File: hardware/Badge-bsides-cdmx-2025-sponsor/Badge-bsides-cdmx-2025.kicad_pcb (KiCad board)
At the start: 2 copper layers, 50 x 110 mm, 30 parts, among them J1 SWDIO, J3 ADDON, J4 Conn_01x04_Pin, J5 I2C, J6 Conn_01x04_Pin, P6 USB_C_Plug_USB2.0, Q3 DMG3415U-7, SW11 ON, SW2 RESET, U1 PY32F030F28U6TR, U6 AP2112K-3.3

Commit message: feat(Hw):started_routing
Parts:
- added C67: 10uF, Capacitor_SMD:C_0603_1608Metric, B.Cu at (-18.5, 29.3)
- added C68: 10uF, Capacitor_SMD:C_0603_1608Metric, B.Cu at (-9.79, 28.9)
- added C69: 10uF, Capacitor_SMD:C_0603_1608Metric, B.Cu at (-27.7, 29.1)
- added C70: 10uF, Capacitor_SMD:C_0603_1608Metric, B.Cu at (-37.4, 30.7)
- added R5: 10k, Resistor_SMD:R_0603_1608Metric, B.Cu at (-18.5, 30.8)
- added R6: 10k, Resistor_SMD:R_0603_1608Metric, B.Cu at (-9.79, 30.4)
- added R7: 10k, Resistor_SMD:R_0603_1608Metric, B.Cu at (-27.7, 30.6)
- added R8: 10k, Resistor_SMD:R_0603_1608Metric, B.Cu at (-37.4, 29.2)
- added SW10: SW_Push, Footprints:TS1088R02026, F.Cu at (-37.3, 29.9)
- added SW7: SW_Push, Footprints:TS1088R02026, F.Cu at (-27.8, 29.9)
- added SW8: SW_Push, Footprints:TS1088R02026, F.Cu at (-18.6, 29.9)
- added SW9: SW_Push, Footprints:TS1088R02026, F.Cu at (-9.34, 29.9)
- BT3, BT4: moved to B.Cu
- J3: moved to F.Cu
- J4: footprint Connector_PinHeader_2.54mm:PinHeader_1x04_P2.54mm_Vertical -> Connector_PinHeader_2.54mm:PinHeader_1x04_P2.54mm_Horizontal; moved to B.Cu
- J6: footprint Connector_PinHeader_2.54mm:PinHeader_1x04_P2.54mm_Vertical -> Connector_PinSocket_2.54mm:PinSocket_1x04_P2.54mm_Horizontal; moved to B.Cu
- moved J1 223.1 mm to (-47.3, 40.9)
- moved J3 190.4 mm to (-44.2, 6.08), turned to 90 degrees
- moved R11 185.4 mm to (-24.3, 41.3), turned to 180 degrees
- moved C33 180.0 mm to (-12.3, 65.4)
- moved D10 179.8 mm to (-24.4, 44.0)
- moved D9 179.8 mm to (-24.1, 67.7), turned to 0 degrees
- moved F3 179.7 mm to (-12.3, 68.4)
- moved J5 179.6 mm to (-47.3, 16.2)
- moved D4 179.5 mm to (-42.1, 71.7)
- moved P6 179.5 mm to (-6.99, 70.8)
- moved Q3 179.5 mm to (-41.6, 75.9)
- moved R10 179.5 mm to (-44.4, 75.9)
- moved SW11 179.5 mm to (-46.7, 70.3)
- moved U1 179.5 mm to (-25.6, 52.5)
- moved C10 179.4 mm to (-37.5, 69.3)
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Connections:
- BT3 pad 2: +3.3V -> +BATT
- J3 pad 5: /GPIO1 -> /GPIO2
- J3 pad 6: /GPIO2 -> /GPIO1
- J4 pad 1: /RX -> GND
- J4 pad 2: /RX -> GND
- J4 pad 3: GND -> /RX
- J4 pad 4: GND -> /RX
- J6 pad 1: /TX -> GND
- J6 pad 2: /TX -> GND
- J6 pad 3: GND -> /TX
- J6 pad 4: GND -> /TX
- U1 pad 1: unconnected-(U1-PA5-Pad1) -> /BTTN2
- U1 pad 10: unconnected-(U1-PB6-Pad10) -> /LED1
- U1 pad 16: /GPIO2 -> /BTTN4
- U1 pad 17: /GPIO1 -> /BTTN3
- U1 pad 2: /LED1 -> /BTTN1
- U1 pad 20: unconnected-(U1-PA4-Pad20) -> /LED2
- U1 pad 3: /LED2 -> /GPIO1
- U1 pad 5: unconnected-(U1-PA12-Pad5) -> /GPIO2
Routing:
- net Net-(BT3--): track 0.00 -> 55.1 mm
- net VBUS: track 0.00 -> 40.2 mm, vias 0 -> 2
- net +BATT: track 0.00 -> 16.9 mm
- net Net-(SW11-A): track 0.00 -> 14.8 mm
- net Net-(F3-Pad1): track 0.00 -> 10.8 mm
- net Net-(D4-K): track 0.00 -> 9.51 mm
- net Net-(P6-CC): track 0.00 -> 7.73 mm
- net Net-(P6-VCONN): track 0.00 -> 6.86 mm
- net +3V3: track 0.00 -> 1.80 mm
- net /BTTN2: track 0.00 -> 1.52 mm
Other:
- board size 50 x 110 mm -> 50.1 x 110 mm

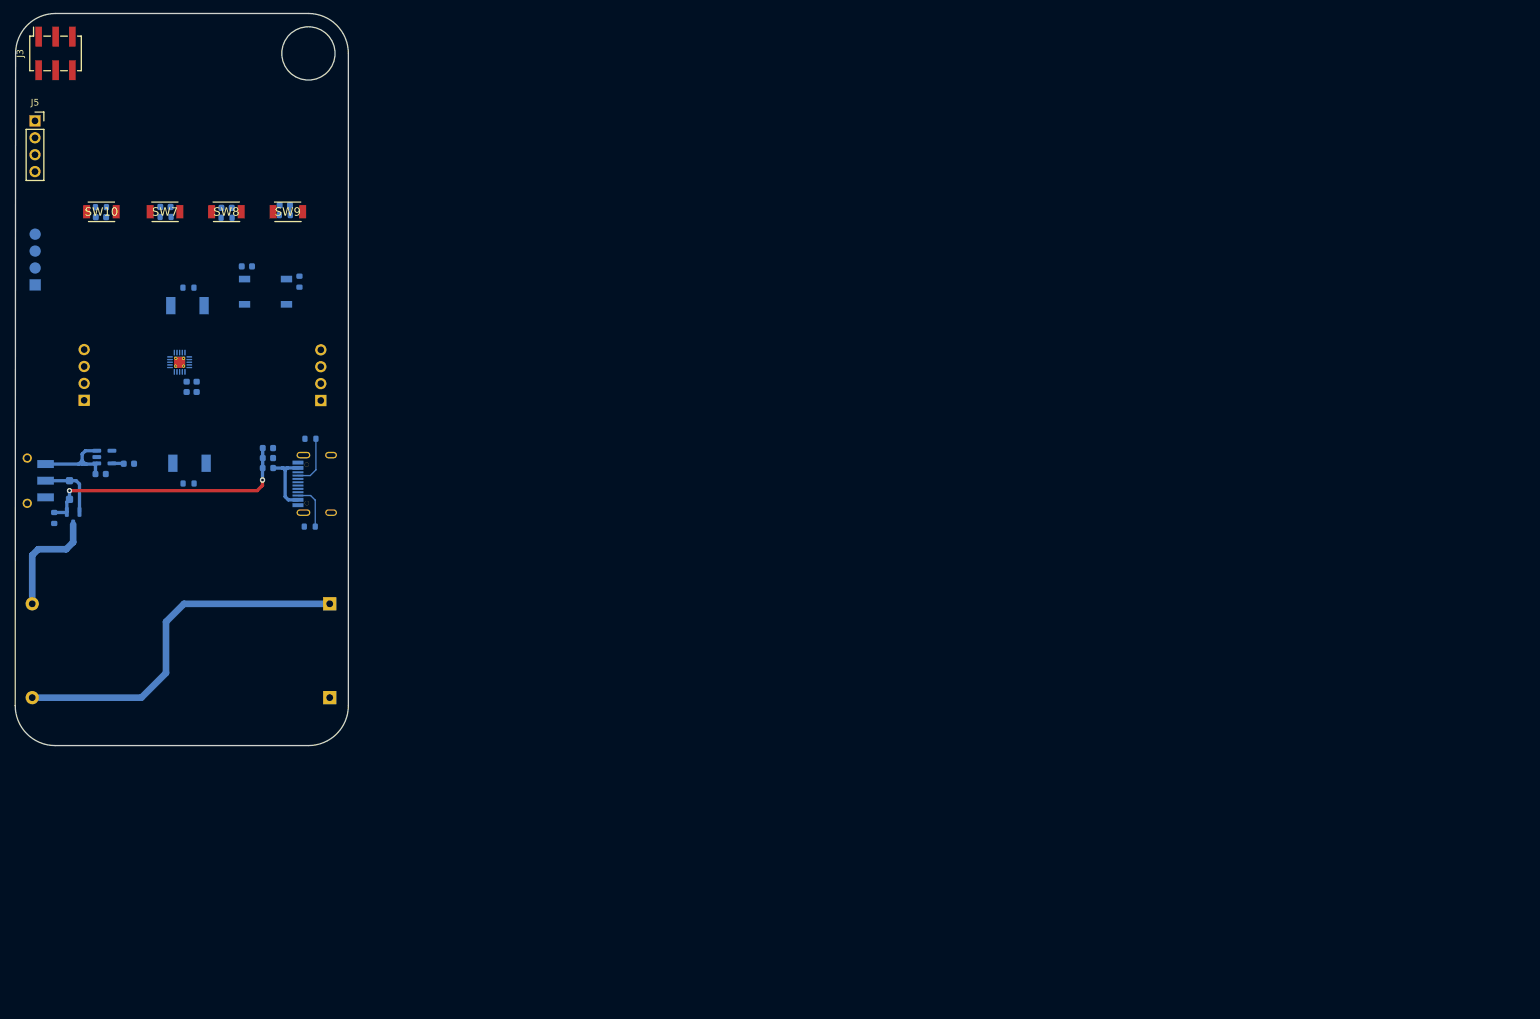
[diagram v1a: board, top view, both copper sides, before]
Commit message: feat(Hw):Route_Sponsor
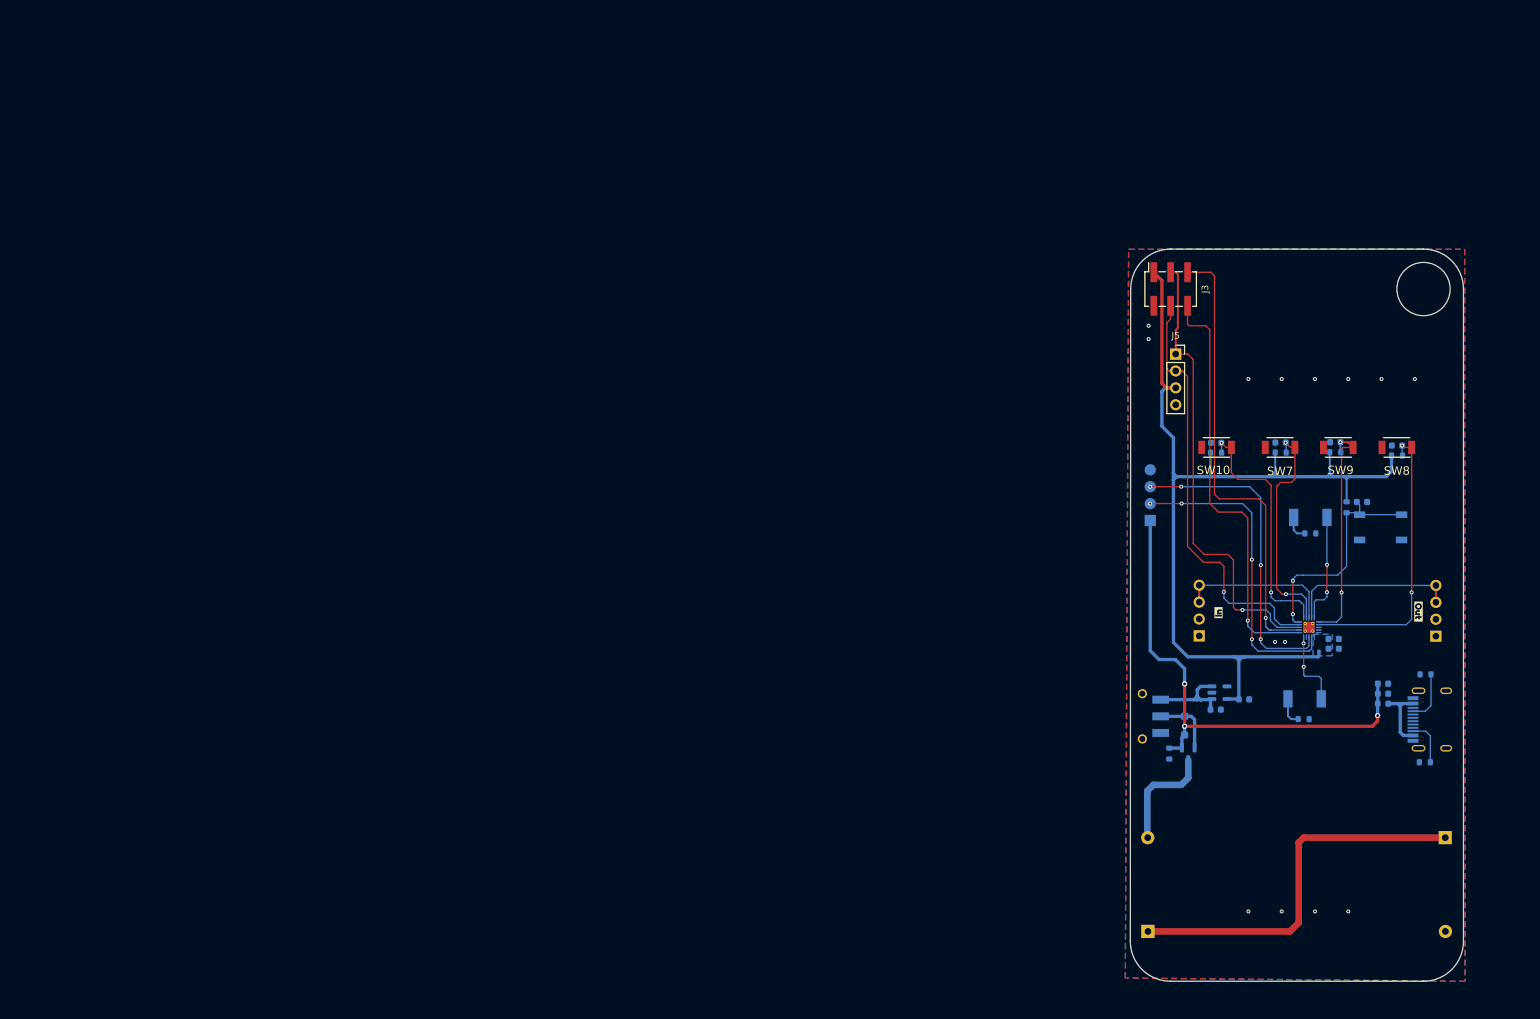
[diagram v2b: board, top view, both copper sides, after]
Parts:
- added kibuzzard-6841D7B6: G***, kibuzzard-6841D7B6, B.Cu at (119.4, 100.2)
- added kibuzzard-6841DB7D: G***, kibuzzard-6841DB7D, B.Cu at (119.2, 111.2)
- added kibuzzard-6841DC13: G***, kibuzzard-6841DC13, B.Cu at (154.8, 81.1)
- added kibuzzard-6841DDA6: G***, kibuzzard-6841DDA6, F.Cu at (130.5, 90.1)
- added kibuzzard-6841DDB3: G***, kibuzzard-6841DDB3, F.Cu at (160.6, 90.0)
- moved C67 179.5 mm to (157.3, 65.0)
- moved R5 179.5 mm to (157.3, 66.5)
- moved SW8 179.4 mm to (157.3, 65.3)
- moved C34 176.8 mm to (147.8, 95.5), turned to 0 degrees
- moved C28 175.0 mm to (147.8, 94.0), turned to 0 degrees
- moved J5 174.9 mm to (124.1, 51.2)
- moved U1 174.3 mm to (144.1, 92.3)
- moved R11 172.6 mm to (144.3, 78.2), turned to 0 degrees
- moved D10 171.7 mm to (144.3, 75.8), turned to 0 degrees
- moved R8 171.6 mm to (130.1, 66.1)
- moved C10 171.2 mm to (130.1, 104.7)
- moved D9 171.2 mm to (143.4, 103.1)
- moved J1 171.2 mm to (120.2, 76.3)
- moved SW11 171.2 mm to (120.8, 105.7)
- moved C26 171.2 mm to (134.3, 103.1)
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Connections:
- BT4 pad 1: GND -> Net-(BT3--)
- BT4 pad 2: Net-(BT3--) -> GND
- C26 pad 1: +3V3 -> +3.3V
- J3 pad 1: +3V3 -> +3.3V
- R4 pad 2: +3V3 -> +3.3V
- R5 pad 2: +3V3 -> +3.3V
- R6 pad 2: +3V3 -> +3.3V
- R7 pad 2: +3V3 -> +3.3V
- R8 pad 2: +3V3 -> +3.3V
- U1 pad 11: unconnected-(U1-PB7-Pad11) -> /GPIO1
- U1 pad 12: unconnected-(U1-PF4/BOOT0-Pad12) -> /GPIO2
- U1 pad 3: /GPIO1 -> unconnected-(U1-PA7-Pad3)
- U1 pad 5: /GPIO2 -> unconnected-(U1-PA12-Pad5)
- U6 pad 5: +3V3 -> +3.3V
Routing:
- net +3.3V: track 0.07 -> 149.9 mm
- net /SDA: track 0.00 -> 69.9 mm, vias 0 -> 1
- net /GPIO2: track 0.00 -> 68.9 mm, vias 0 -> 1
- net /SCL: track 0.00 -> 64.2 mm, vias 0 -> 1
- net /GPIO1: track 0.00 -> 63.5 mm, vias 0 -> 1
- net /SWCLK: track 0.00 -> 48.2 mm, vias 0 -> 4
- net /SWDIO: track 0.00 -> 47.0 mm, vias 0 -> 4
- net /BTTN1: track 0.00 -> 43.2 mm, vias 0 -> 2
- net /BTTN4: track 0.00 -> 37.9 mm, vias 0 -> 2
- net /NTST: track 0.00 -> 34.6 mm, vias 0 -> 2
- net VBUS: track 40.2 -> 74.7 mm, vias 2 -> 3
- net /BTTN3: track 0.00 -> 34.4 mm, vias 0 -> 2
- net /BTTN2: track 1.52 -> 34.6 mm, vias 0 -> 2
- net /RX: track 0.00 -> 25.5 mm
- net /TX: track 0.00 -> 23.3 mm
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- added copper zone on B.Cu, net +3.3V
- added copper zone on B.Cu, net GND
- added copper zone on F.Cu, net GND

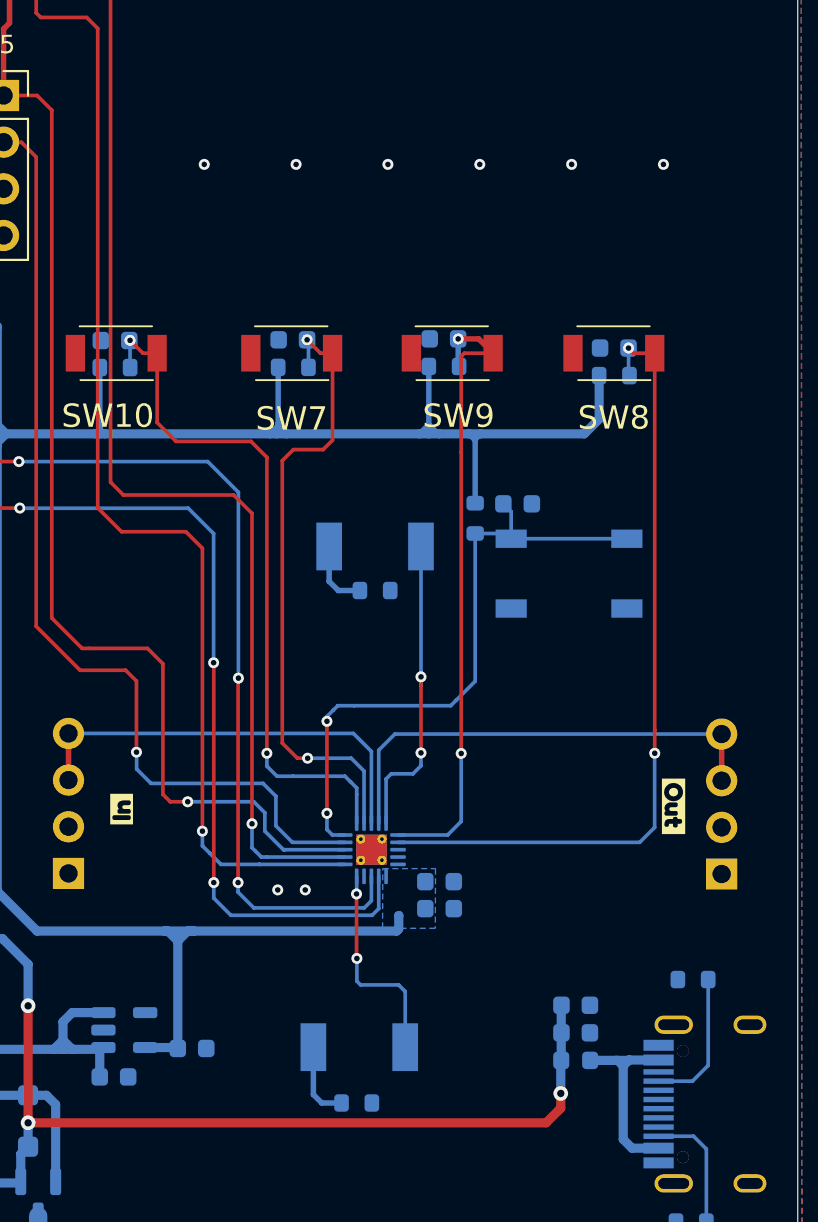
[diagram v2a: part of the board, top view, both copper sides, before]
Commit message: feat(Hw):Neopixels_added(sponsor)
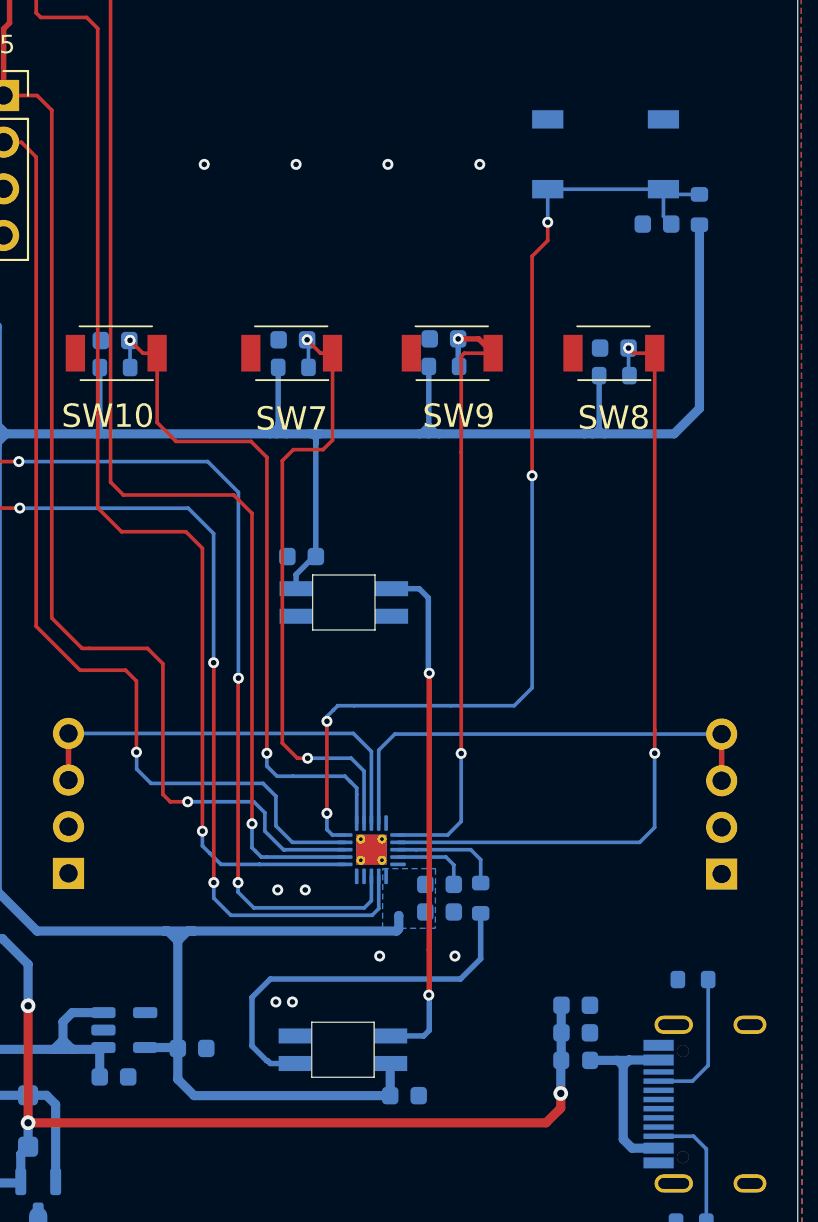
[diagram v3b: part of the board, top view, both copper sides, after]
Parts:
- removed D10, D9: R_LED, Footprints:LYT77K-K2M1
- removed R11, R9: 220, Resistor_SMD:R_0603_1608Metric
- added C29: 100nF, Capacitor_SMD:C_0603_1608Metric, B.Cu at (145.9, 105.7)
- added C30: 100nF, Capacitor_SMD:C_0603_1608Metric, B.Cu at (140.3, 76.3)
- added D19: WS2812B, Footprints:LED_SK6812-E, B.Cu at (142.6, 103.2)
- added D20: WS2812B, Footprints:LED_SK6812-E, B.Cu at (142.6, 78.8)
- added R3: 1K, Resistor_SMD:R_0603_1608Metric, B.Cu at (150.1, 95.0)
- added kibuzzard-6842C085: G***, kibuzzard-6842C085, B.Cu at (135.3, 124.3)
- kibuzzard-6841DDA6, kibuzzard-6841DDB3: moved to B.Cu
- moved SW2 22.9 mm to (156.8, 54.5), turned to 180 degrees
- moved kibuzzard-6841DC13 22.9 mm to (156.4, 58.2)
- moved R4 20.8 mm to (162.0, 57.5), turned to -90 degrees
- moved C6 17.0 mm to (159.7, 58.2), turned to 180 degrees
- moved C34 0.18 mm to (147.8, 95.7)
- moved C28 0.15 mm to (147.8, 94.2)
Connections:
- U1 pad 10: /LED1 -> unconnected-(U1-PB6-Pad10)
- U1 pad 20: /LED2 -> unconnected-(U1-PA4-Pad20)
- U1 pad 3: unconnected-(U1-PA7-Pad3) -> /NEO
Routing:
- net +3.3V: track 149.9 -> 188.2 mm
- net Net-(D19-DOUT): track 0.00 -> 28.0 mm, vias 0 -> 2
- net /NTST: track 34.6 -> 57.0 mm, vias 2 -> 4
- net Net-(D19-DIN): track 0.00 -> 21.2 mm
- net /LED2: track 17.0 -> 0.00 mm, vias 2 -> 0
- net /LED1: track 11.6 -> 0.00 mm, vias 2 -> 0
- net /NEO: track 0.00 -> 6.00 mm
- net Net-(D9-K): track 4.31 -> 0.00 mm
- net GND: track 0.00 -> 4.28 mm, vias 14 -> 16
- net Net-(D10-K): track 3.78 -> 0.00 mm

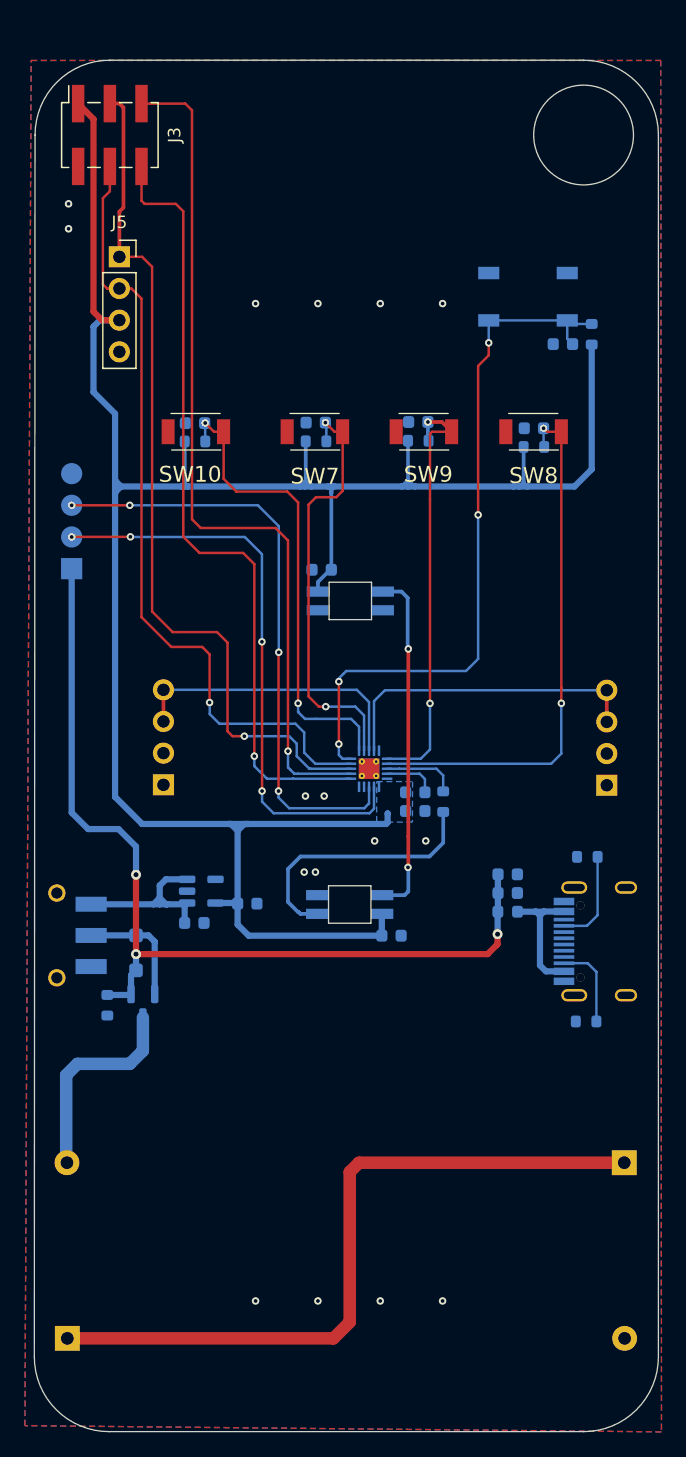
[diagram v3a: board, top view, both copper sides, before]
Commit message: Feat(Hw): Fixed_Bom(Sponsor,guest)
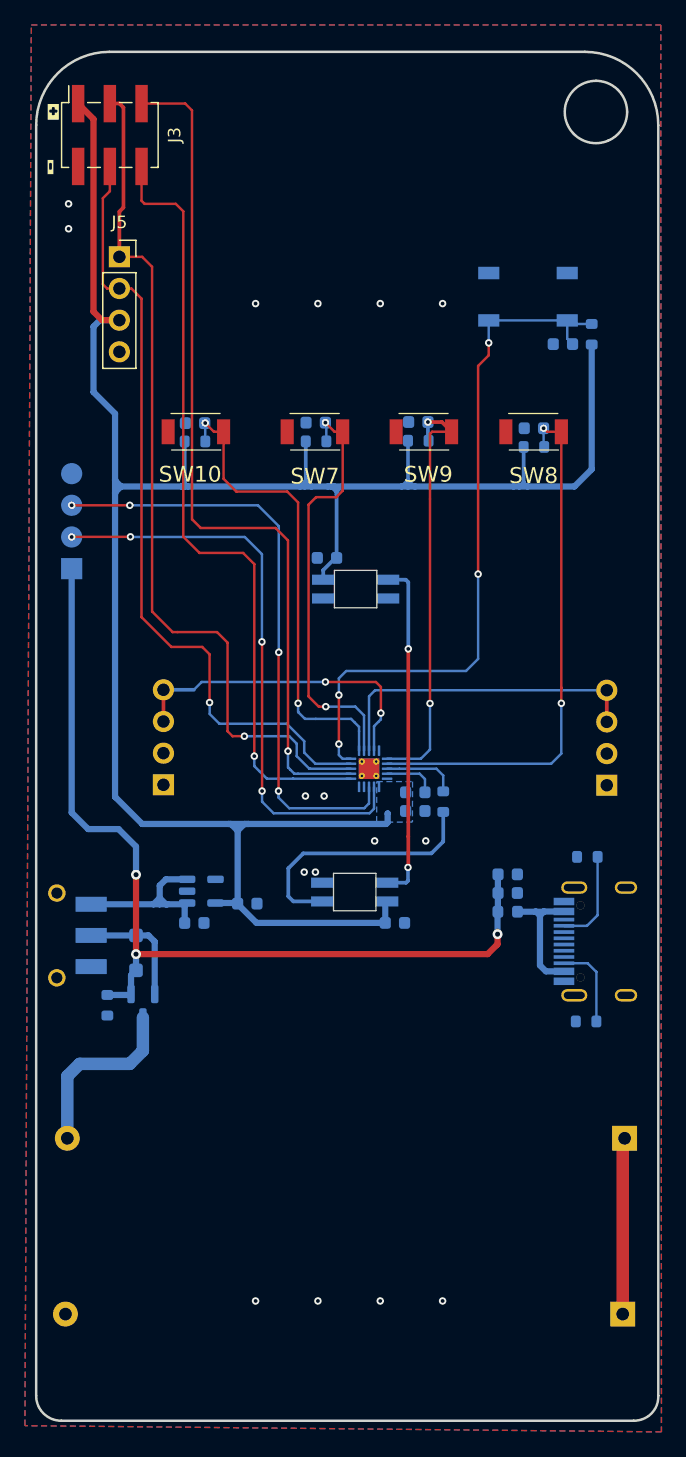
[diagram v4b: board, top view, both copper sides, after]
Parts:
- added kibuzzard-6842ED2D: G***, kibuzzard-6842ED2D, B.Cu at (120.5, 56.3)
- added kibuzzard-6842ED45: G***, kibuzzard-6842ED45, B.Cu at (120.4, 59.1)
- added kibuzzard-6842EE28: G***, kibuzzard-6842EE28, F.Cu at (118.8, 39.6)
- added kibuzzard-6842EE36: G***, kibuzzard-6842EE36, F.Cu at (118.5, 44.0)
- moved BT4 44.6 mm to (164.4, 136.1), turned to 180 degrees
- moved BT3 1.96 mm to (119.9, 122.0)
- moved D19 1.08 mm to (142.9, 102.2)
- moved C29 1.06 mm to (146.2, 104.7)
- moved D20 1.04 mm to (143.0, 77.9)
- moved C30 1.04 mm to (140.7, 75.4)
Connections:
- J4 pad 3: /RX -> /TX
- J4 pad 4: /RX -> /TX
- J6 pad 3: /TX -> /RX
- J6 pad 4: /TX -> /RX
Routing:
- net Net-(BT3--): track 57.7 -> 14.2 mm
- net /TX: track 23.3 -> 26.2 mm
- net +BATT: track 16.9 -> 14.6 mm
- net +3.3V: track 188.2 -> 185.9 mm
- net Net-(D19-DOUT): track 28.0 -> 27.5 mm
- net /RX: track 25.5 -> 25.7 mm, vias 0 -> 2
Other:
- board size 50.1 x 110 mm -> 49.9 x 109.8 mm
